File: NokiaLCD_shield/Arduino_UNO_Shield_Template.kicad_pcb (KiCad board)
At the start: 2 copper layers, 78.7 x 53.3 mm, 12 parts, among them CON1 Nokia1616_LCD, CON2 Micro_SD_Card, P1 CONN_01X02, Q1 BC548, U1 ArduinoUnoR3

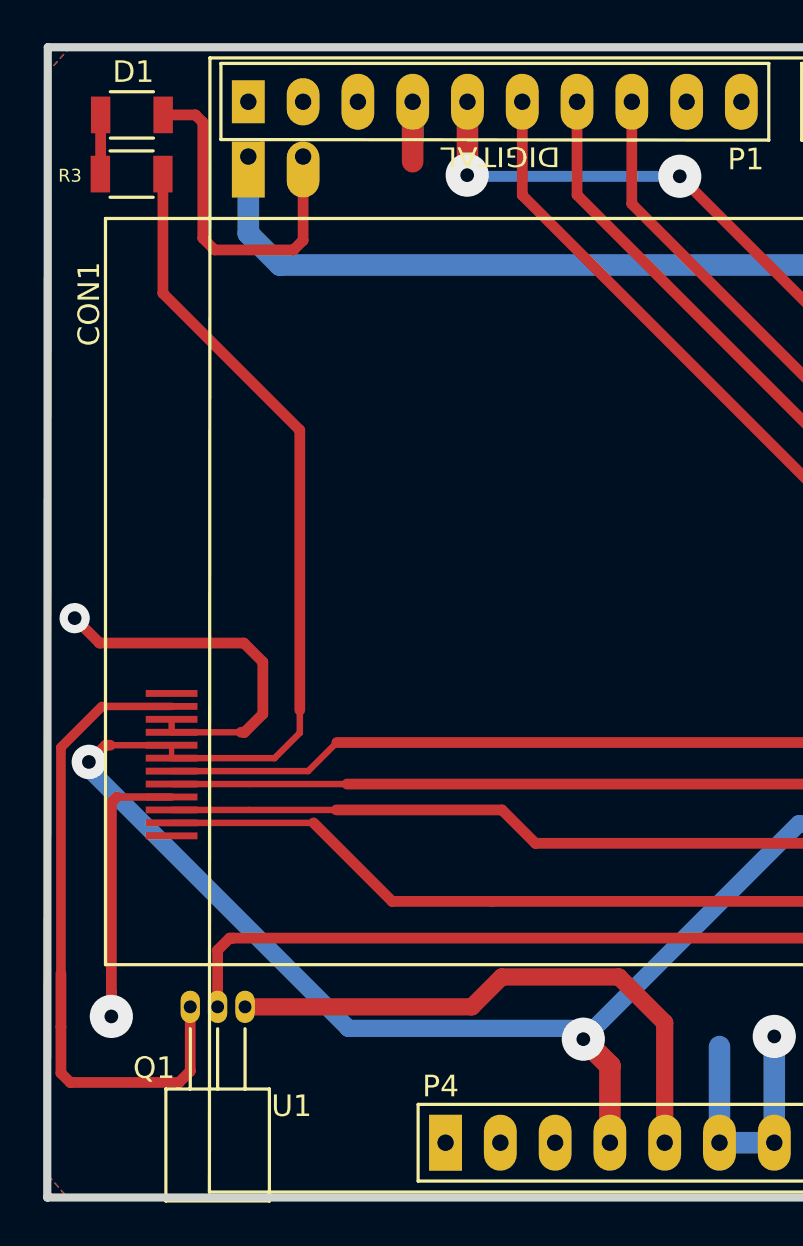
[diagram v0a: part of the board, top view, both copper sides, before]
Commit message: Add arduino flex-sensor and SW2812B LED shields Add a folder for a flex-snsor arduino shield Add a folder for SW2812B LEDs arduino shield with a 4-channel 5v-3.3v levelshifter
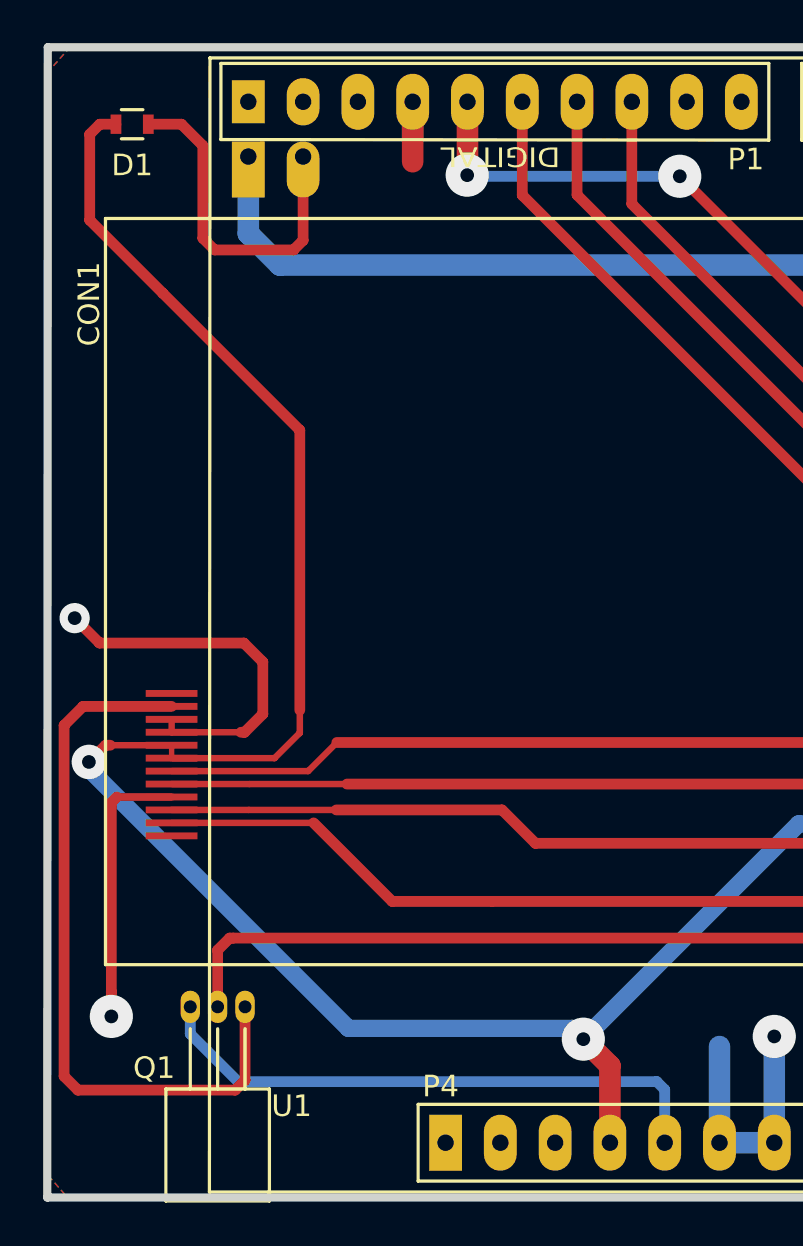
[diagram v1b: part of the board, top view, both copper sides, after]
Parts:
- removed R3: 10K, Resistors_SMD:R_1206
- D1: footprint Resistors_SMD:R_1206 -> Resistors_SMD:R_0603
- moved D1 0.43 mm to (48.7, 76.2)
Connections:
- D1 pad 2: Net-(D1-Pad2) -> 3.3V
- Q1 pad 1: LED+ -> 5V
- Q1 pad 3: 5V -> LED+
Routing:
- net 3.3V: track 115.2 -> 119.9 mm
- net LED+: track 30.4 -> 33.9 mm
- net Net-(D1-Pad2): track 2.75 -> 0.00 mm

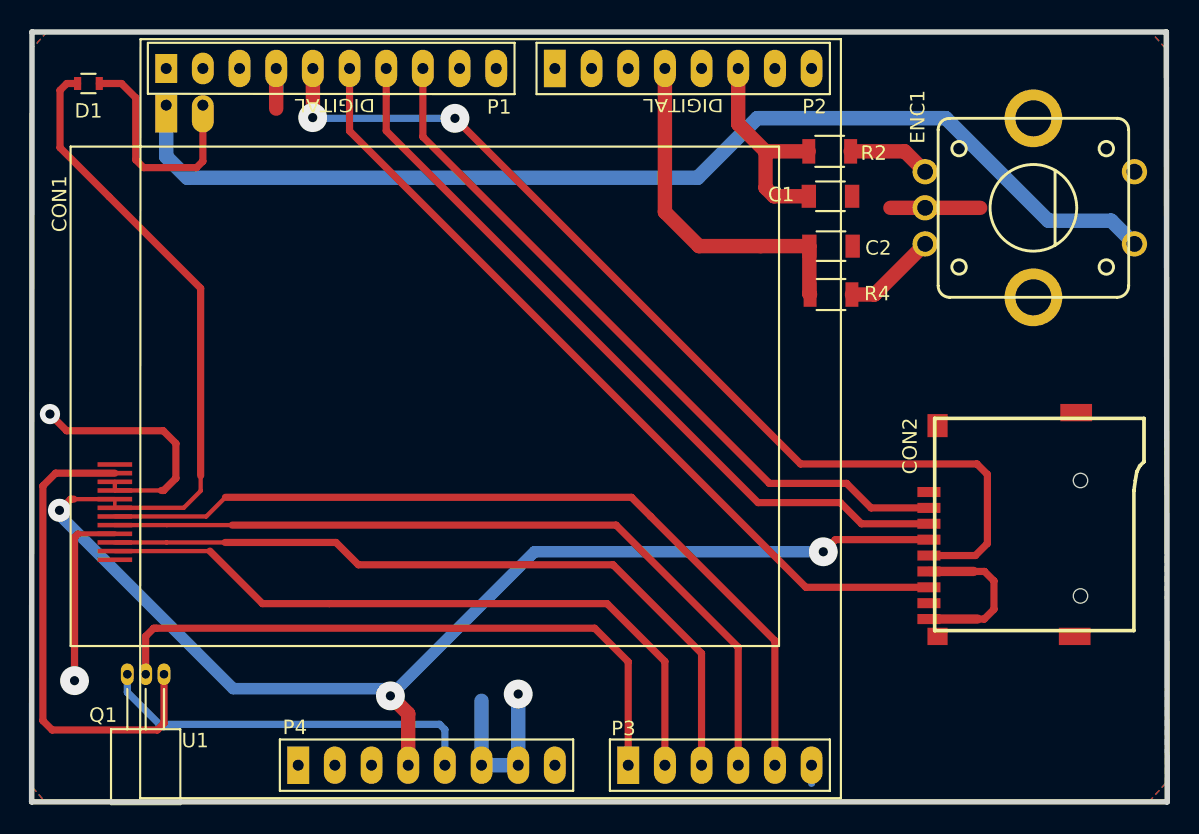
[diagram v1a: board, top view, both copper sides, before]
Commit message: Changed Nokia1616 LCD backlight Added a low switch NPN transistor for PWM switching of backlight to ground Added a capacitor to ground on the 3v3 line Cleaned up the traces a bit
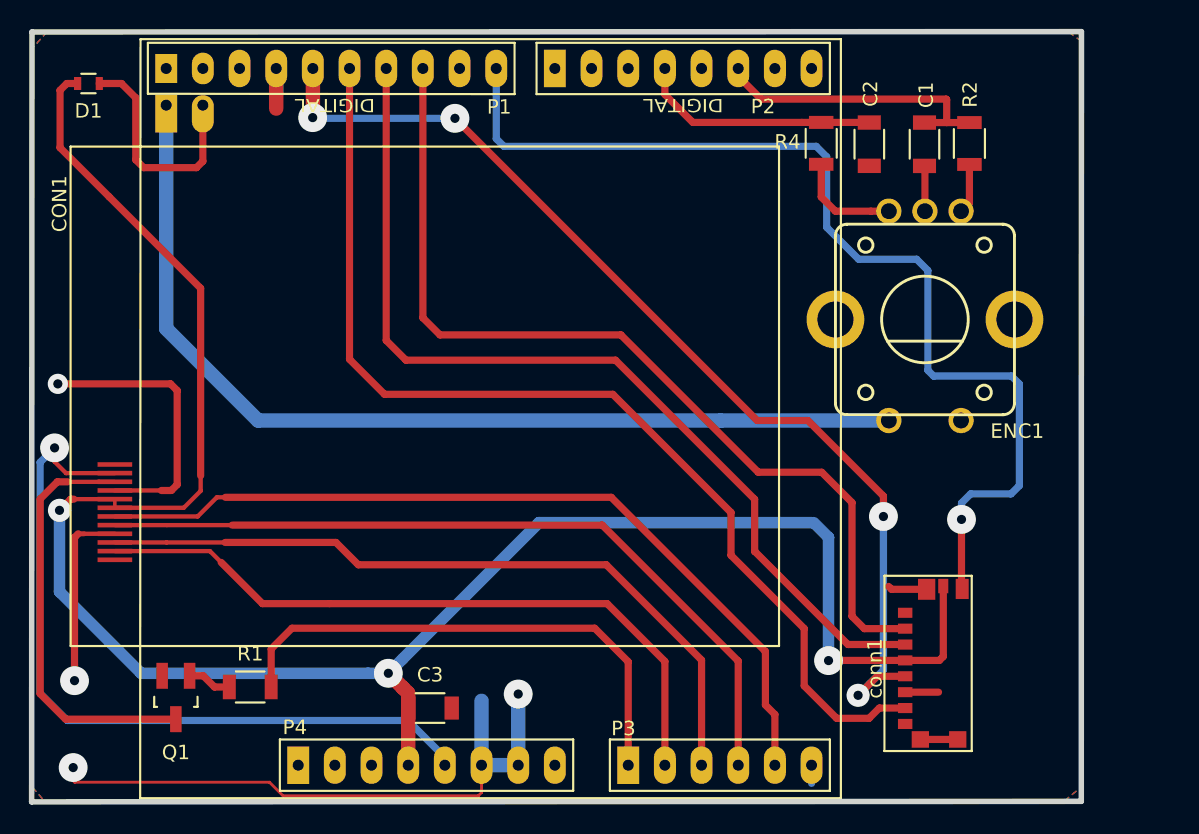
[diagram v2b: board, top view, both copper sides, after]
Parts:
- removed CON2: Micro_SD_Card, Connect:micro-SDcard
- added C3: 0.1uF, Capacitors_SMD:C_1206, F.Cu at (72.4, 119.5)
- added R1: 1K, Resistors_SMD:R_1206, F.Cu at (59.9, 118.0)
- added conn1: sdcard_475710001, Connect:MicroSDcard-475710001, F.Cu at (104.0, 116.7)
- C1, C2: value 0.01uF -> 0.1uF
- Q1: value BC548 -> BC547_BEC_123; footprint TO_SOT_Packages_THT:TO-92_Horizontal1_Inline_Narrow_Oval -> TO_SOT_Packages_SMD:SOT-23_Handsoldering
- moved ENC1 10.8 mm to (106.7, 92.6), turned to 180 degrees
- moved R4 10.5 mm to (99.5, 80.4), turned to 90 degrees
- moved R2 9.69 mm to (109.7, 80.4), turned to 90 degrees
- moved C2 7.54 mm to (102.8, 80.4), turned to 270 degrees
- moved C1 7.45 mm to (106.6, 80.4), turned to 270 degrees
- moved Q1 3.73 mm to (54.8, 118.8), turned to 180 degrees
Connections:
- CON1 pad 10: GND -> LED-
- CON1 pad 11: LED+ -> 5V
- Q1 pad 1: 5V -> Net-(Q1-Pad1)
- Q1 pad 2: AD0 -> GND
- Q1 pad 3: LED+ -> LED-
- U1 pad 10: (no net) -> IO8
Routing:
- net IO8: track 0.00 -> 72.6 mm, vias 0 -> 1
- net LED+: track 33.9 -> 0.00 mm
- net LED-: track 0.00 -> 29.3 mm
- net GND: track 64.2 -> 91.2 mm, vias 3 -> 4
- net 5V: track 26.8 -> 53.3 mm, vias 0 -> 1
- net 3.3V: track 119.9 -> 139.8 mm
- net IO12/MISO: track 57.6 -> 73.3 mm
- net IO10/SS: track 50.4 -> 64.2 mm
- net IO11/MOSI: track 53.2 -> 65.6 mm
- net Net-(ENC1-PadSW2): track 76.6 -> 68.2 mm
- net AD0: track 44.4 -> 36.1 mm
- net IO4: track 24.3 -> 16.8 mm
- net IO2: track 15.3 -> 20.3 mm
- net Net-(Q1-Pad1): track 0.00 -> 3.07 mm
- net IO13/SCK: track 69.6 -> 72.1 mm, vias 2 -> 4
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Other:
- board size 78.7 x 53.3 mm -> 72.7 x 53.4 mm
